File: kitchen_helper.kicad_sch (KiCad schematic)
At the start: 20 parts, among them IC1 ESP32-S3-WROOM-1-N8R8, J2 PROG_HDR, Q1 SS8050-G, Q2 SS8050-G, SW1 SW_Reset

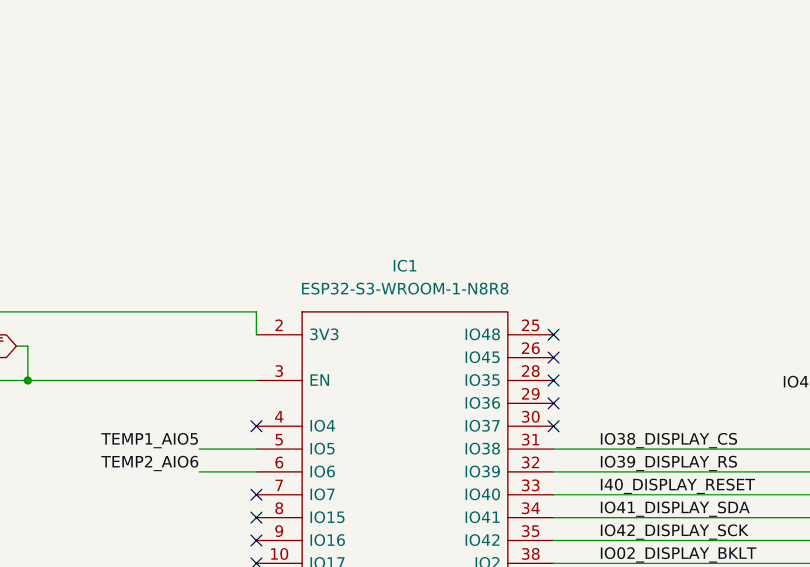
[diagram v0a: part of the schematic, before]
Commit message: Migrated project to KiCad7
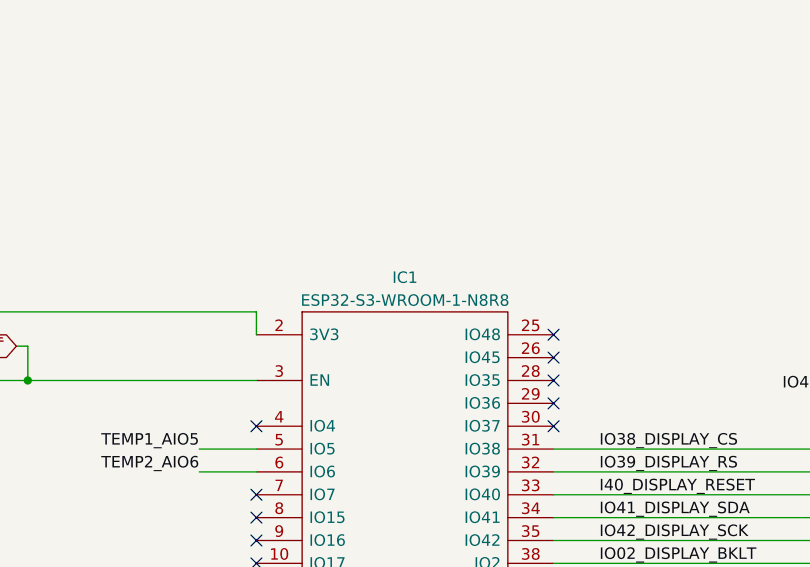
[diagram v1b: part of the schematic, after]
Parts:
- IC1: footprint footprints:ESP32S3WROOM1N8R8 -> ESP32S3WROOM1N8R8; symbol ESP32-S3-WROOM-1-N8R8:ESP32-S3-WROOM-1-N8R8 -> MCU_Espressif:ESP32-S3-WROOM-1-N8R8
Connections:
- net +3V3: no longer J2.1 (Pin_1)
- new net +3.3V: J2.1 (Pin_1)
